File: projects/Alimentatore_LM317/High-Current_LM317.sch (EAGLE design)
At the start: 17 parts, among them X1 SMKDSP_1,5/3, X2 SMKDSP_1,5/3, X3 SMKDSP_1,5/3

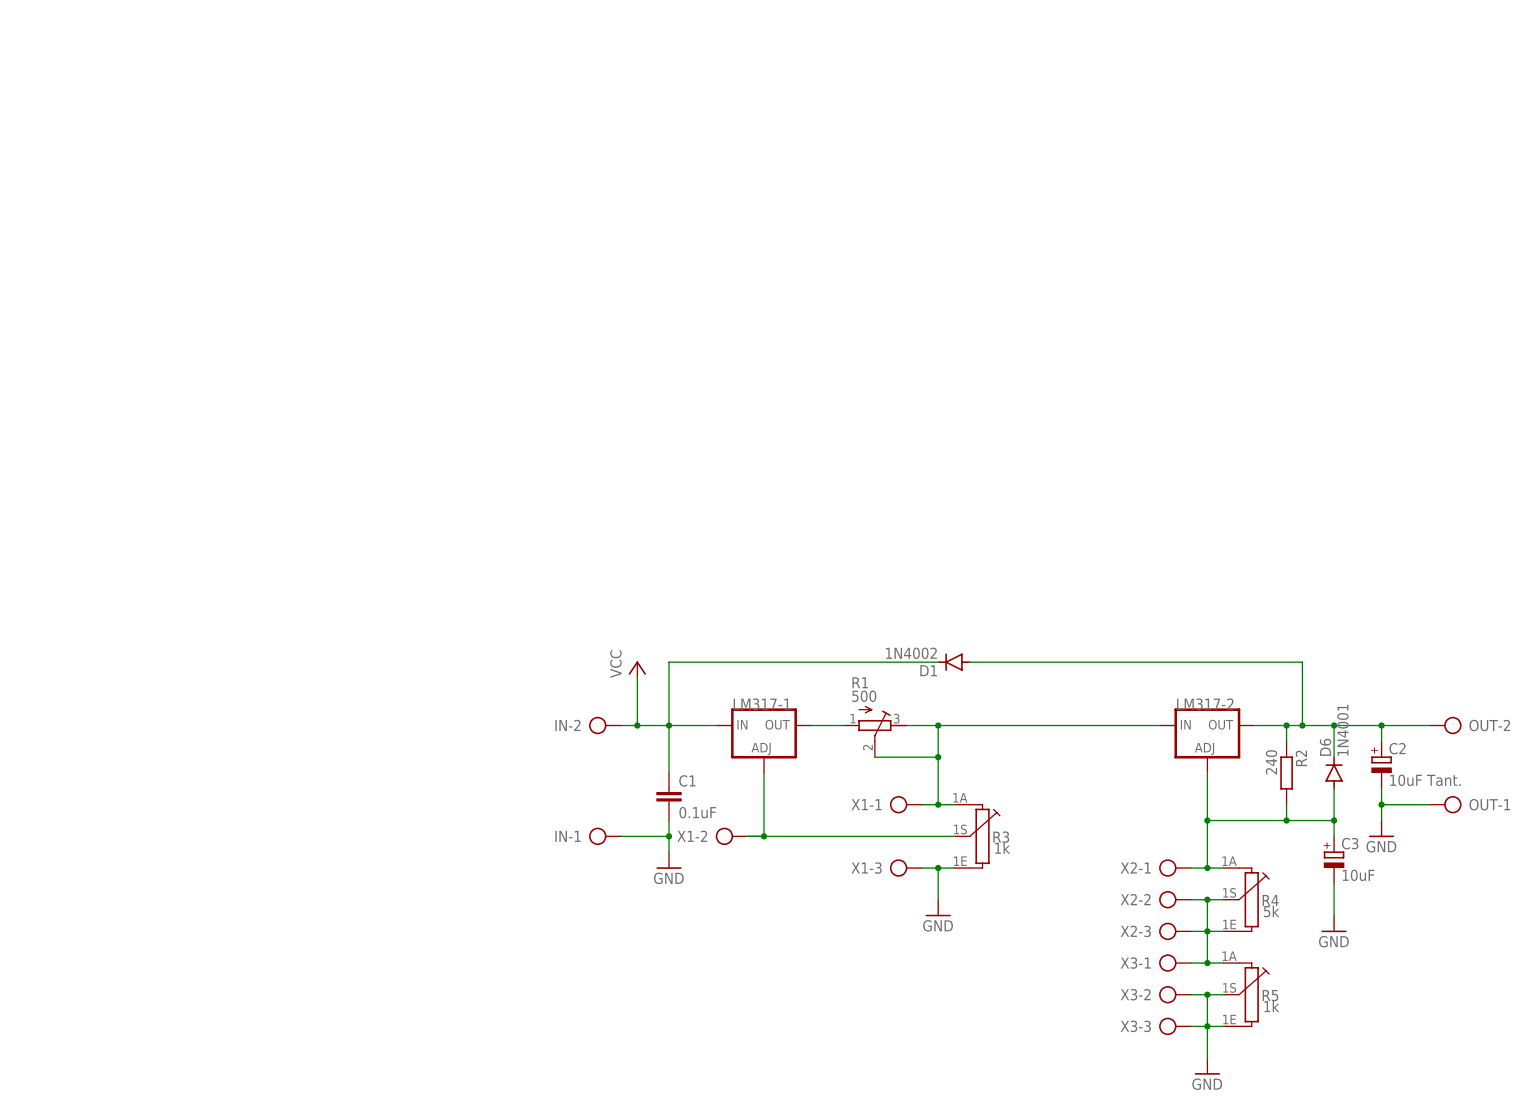
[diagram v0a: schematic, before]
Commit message: aggiunti circuiti alternativi LM317.
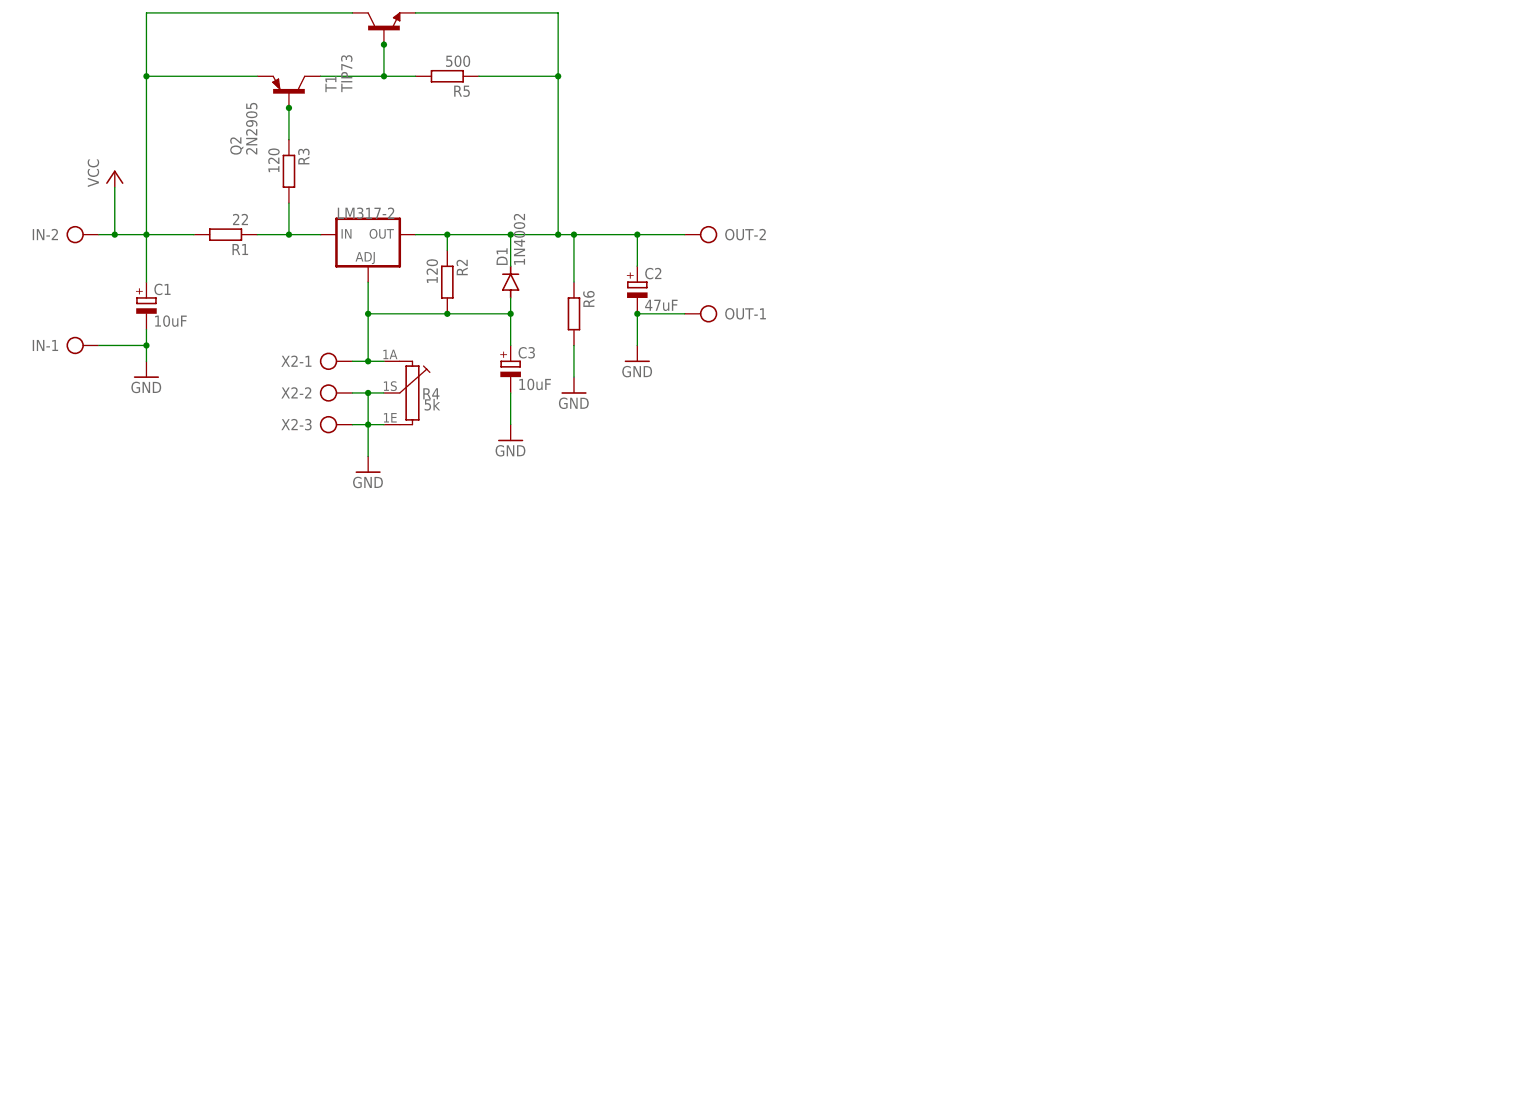
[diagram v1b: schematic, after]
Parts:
- removed D6: 1N4001, diode_MOD:1N4004DO-41
- removed LM317-1: (no value), v-reg:LM317TS317TS_TO220
- removed X1, X3: SMKDSP_1,5/3, con-phoenix-smkdsp:SMKDSP_1,5/3
- added Q2: 2N2905, transistor-pnp:2N2905
- added R6: (no value), rcl:R-EU_0204/7
- added T1: TIP73, transistor:2N1613
- C1: value 0.1uF -> 10uF; device rcl:C-EU025-024X044 -> rcl:CPOL-EUE2-5
- C2: value 10uF Tant. -> 47uF
- R1: value 500 -> 22; device rcl:R-TRIMM4G/J -> rcl:R-EU_0204/7
- R2: value 240 -> 120
- R3: value 1k -> 120; device piher:PC16S -> rcl:R-EU_0204/7
- R5: value 1k -> 500; device piher:PC16S -> rcl:R-EU_0204/7
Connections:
- removed net N$4: R4.1E, R4.1S, R5.1A, X2-2.KL, X2-3.KL, X3-1.KL
- net GND: now also C1.-, R4.1E, R4.1S, R6.2, X2-2.KL, X2-3.KL; no longer C1.2, R3.1E, R5.1E, R5.1S, X1-3.KL, X3-2.KL, X3-3.KL
- net N$1: now also D1.C, R5.1, R6.1, T1.E; no longer D1.A, D6.C
- net N$2: now also LM317-2.IN, R1.1, R3.2; no longer LM317-1.OUT, R1.A
- net N$3: now also Q2.B, R3.1; no longer LM317-2.IN, R1.E, R1.S, R3.1A, X1-1.KL
- net N$5: now also Q2.C, R5.2, T1.B; no longer LM317-1.ADJ, R3.1S, X1-2.KL
- net N$9: now also D1.A; no longer D6.A
- net VCC: now also C1.+, Q2.E, R1.2, T1.C; no longer C1.1, D1.C, LM317-1.IN
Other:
- moved on the sheet: C2, C3, D1, IN-1, IN-2, LM317-2, OUT-1, OUT-2, R2, R4, X2-1, X2-2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
